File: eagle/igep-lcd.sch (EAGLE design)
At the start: 9 parts, among them IC1 LM1117IMPX-3.3, U1 SN74LVC8T245PW, U2 SN74LVC8T245PW, U3 SN74LVC8T245PW, U4 SN74LVC8T245PW

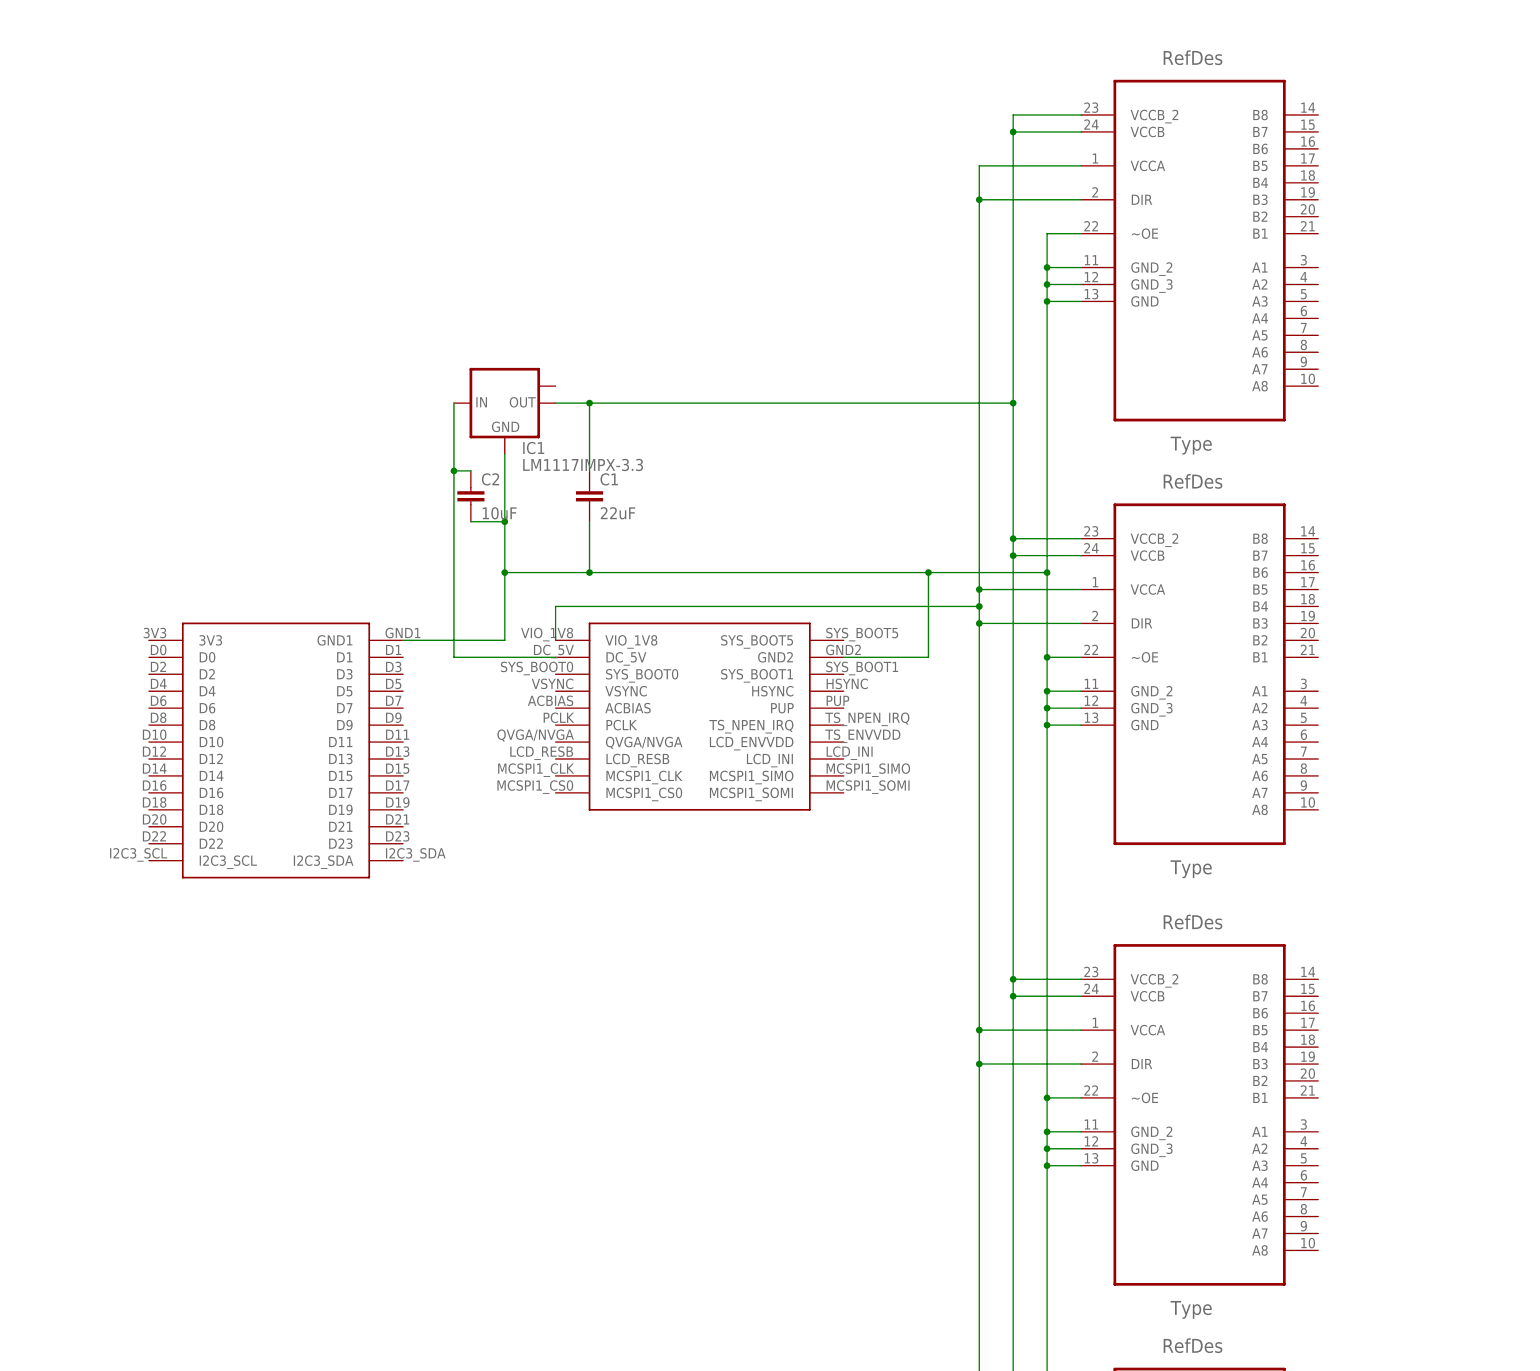
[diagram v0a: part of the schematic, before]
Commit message: Added LCD data bus to level shifters
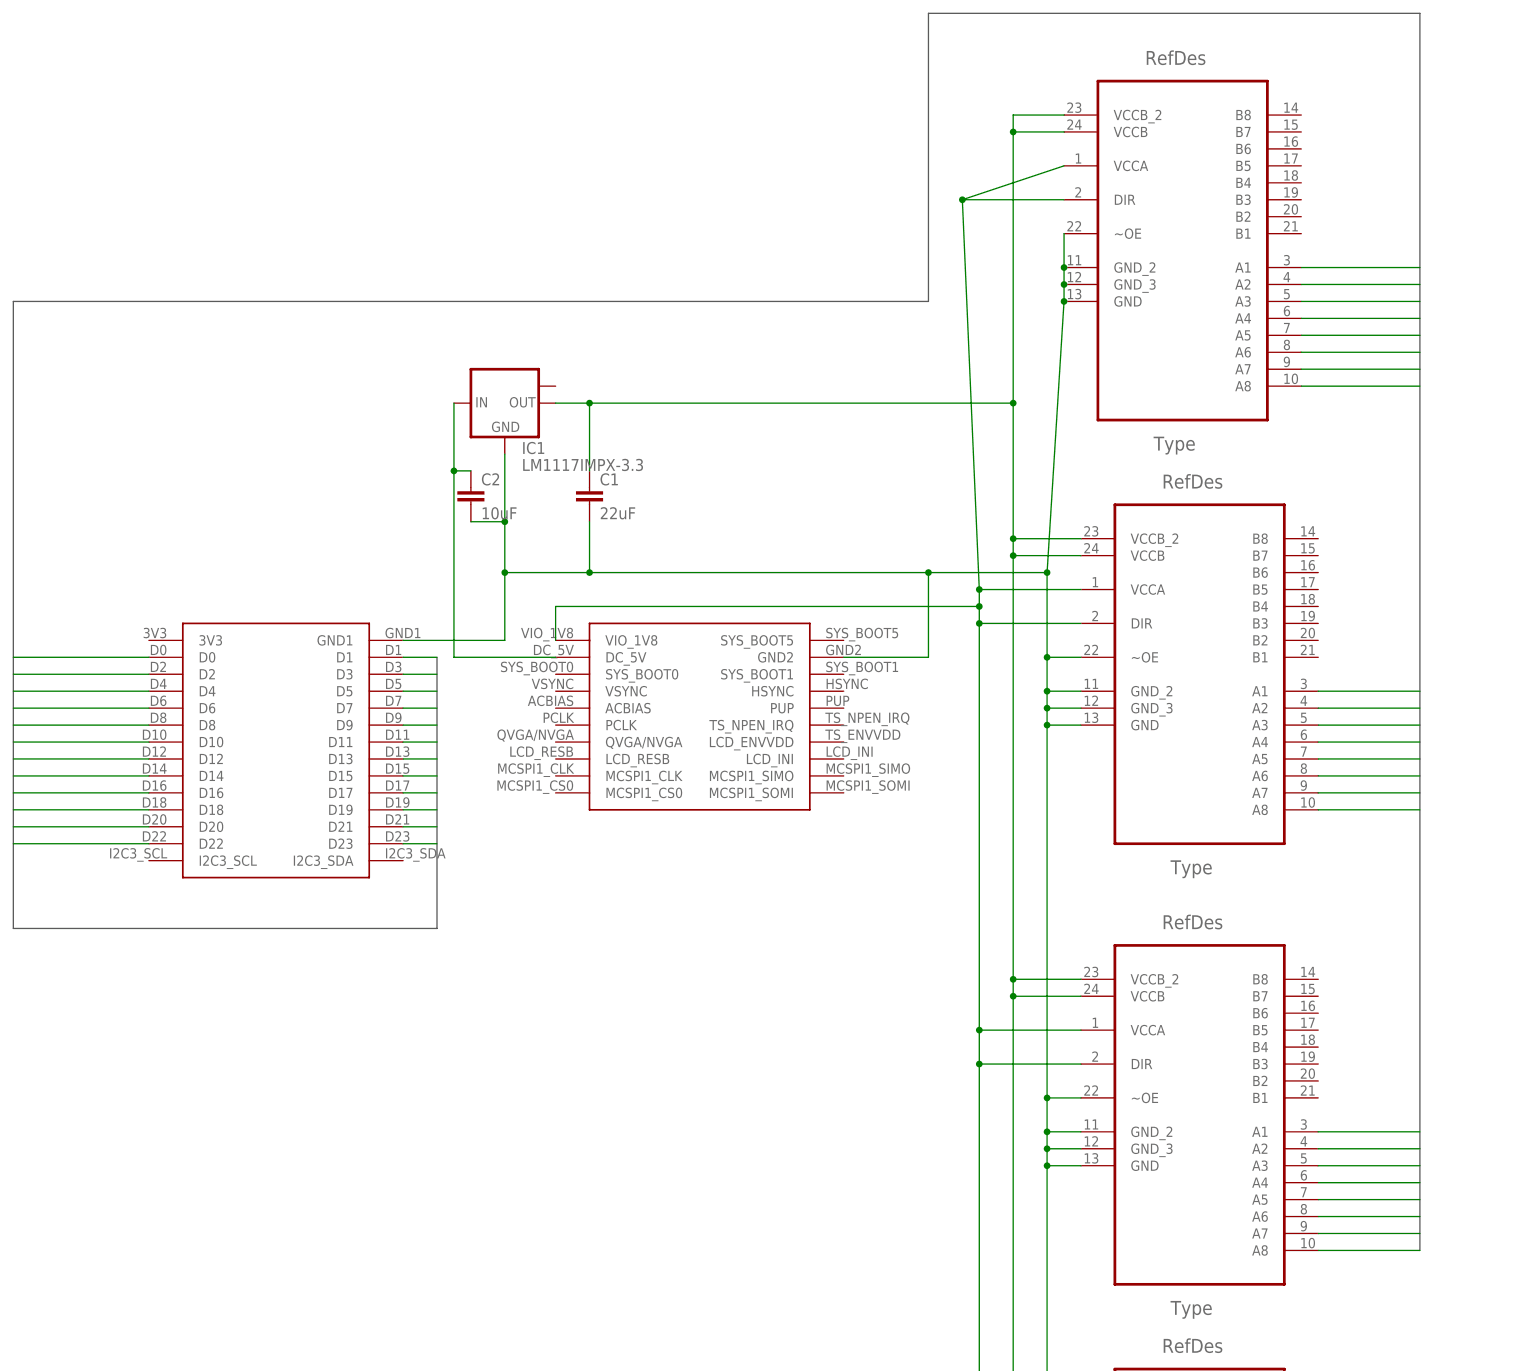
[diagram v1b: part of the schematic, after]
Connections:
- new net LCD_DATA0: U$1.D0, U1.A1
- new net LCD_DATA1: U$1.D1, U1.A2
- new net LCD_DATA10: U$1.D10, U2.A3
- new net LCD_DATA11: U$1.D11, U2.A4
- new net LCD_DATA12: U$1.D12, U2.A5
- new net LCD_DATA13: U$1.D13, U2.A6
- new net LCD_DATA14: U$1.D14, U2.A7
- new net LCD_DATA15: U$1.D15, U2.A8
- new net LCD_DATA16: U$1.D16, U3.A1
- new net LCD_DATA17: U$1.D17, U3.A2
- new net LCD_DATA18: U$1.D18, U3.A3
- new net LCD_DATA19: U$1.D19, U3.A4
- new net LCD_DATA2: U$1.D2, U1.A3
- new net LCD_DATA20: U$1.D20, U3.A5
- new net LCD_DATA21: U$1.D21, U3.A6
- new net LCD_DATA22: U$1.D22, U3.A7
- new net LCD_DATA23: U$1.D23, U3.A8
- new net LCD_DATA3: U$1.D3, U1.A4
- new net LCD_DATA4: U$1.D4, U1.A5
- new net LCD_DATA5: U$1.D5, U1.A6
- new net LCD_DATA6: U$1.D6, U1.A7
- new net LCD_DATA7: U$1.D7, U1.A8
- new net LCD_DATA8: U$1.D8, U2.A1
- new net LCD_DATA9: U$1.D9, U2.A2

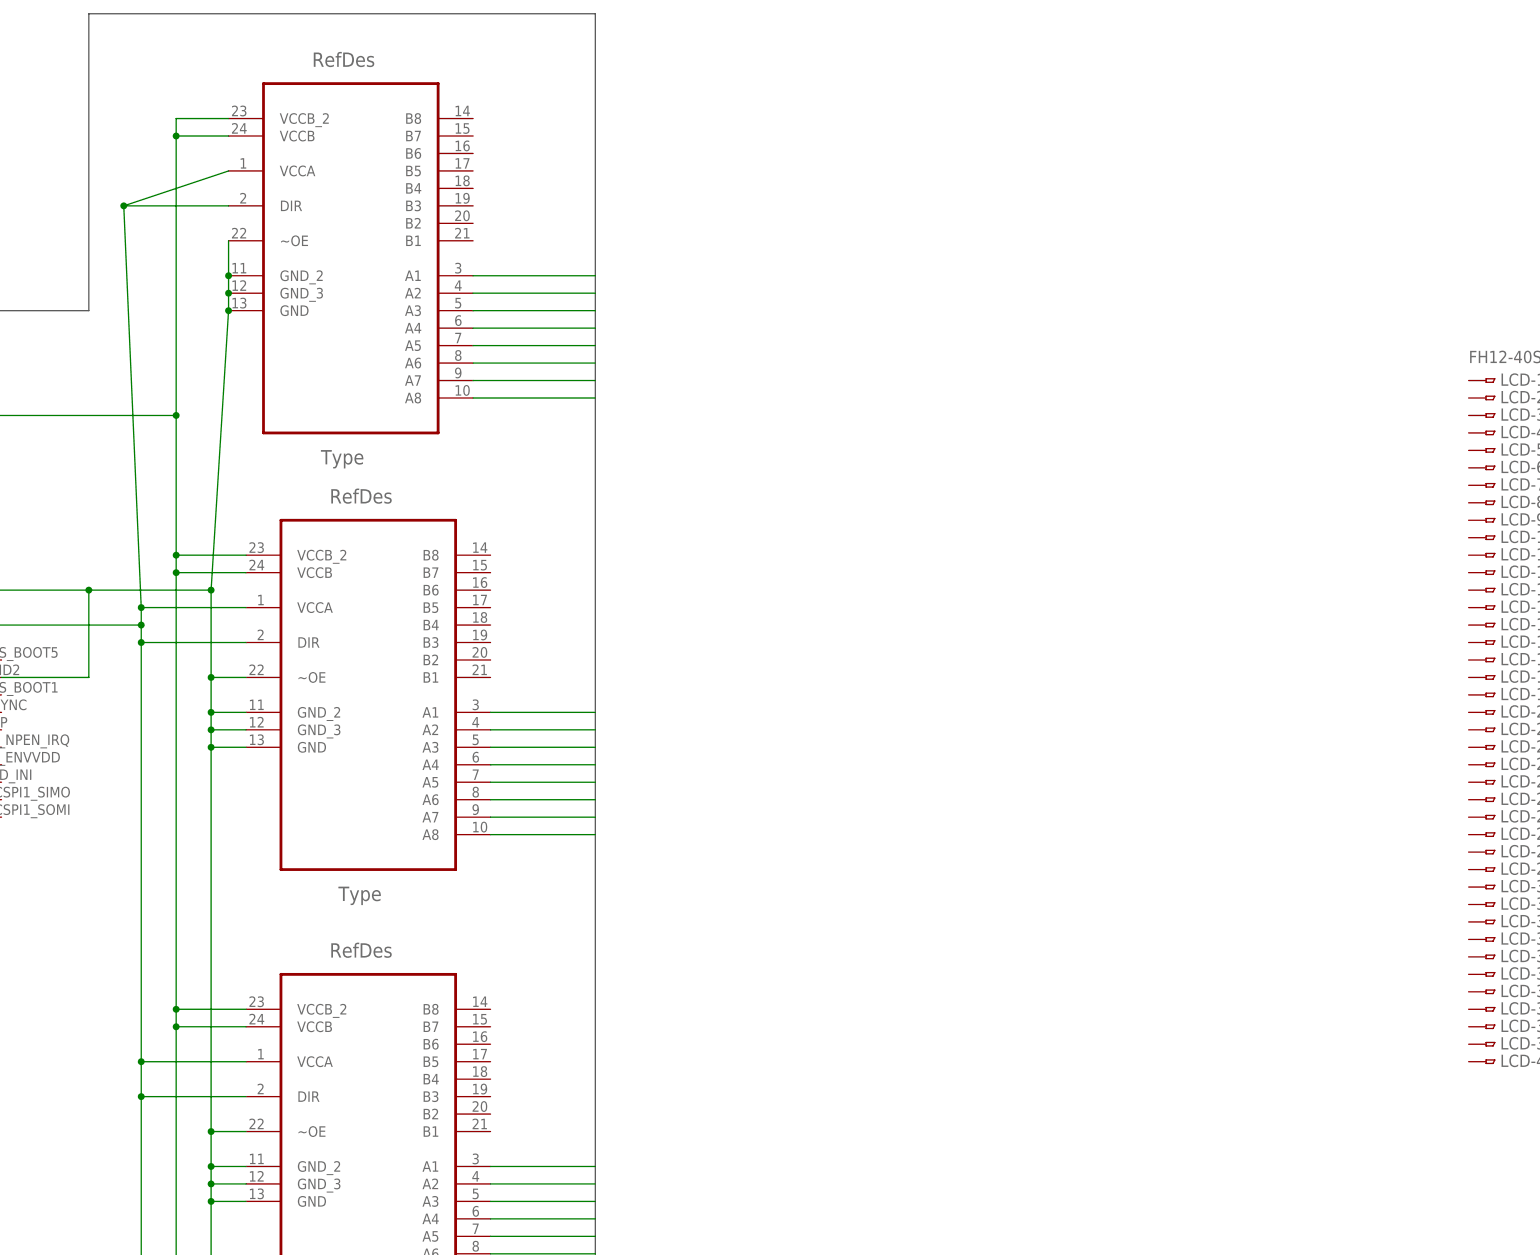
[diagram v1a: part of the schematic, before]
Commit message: Igep lcd data to level shifters
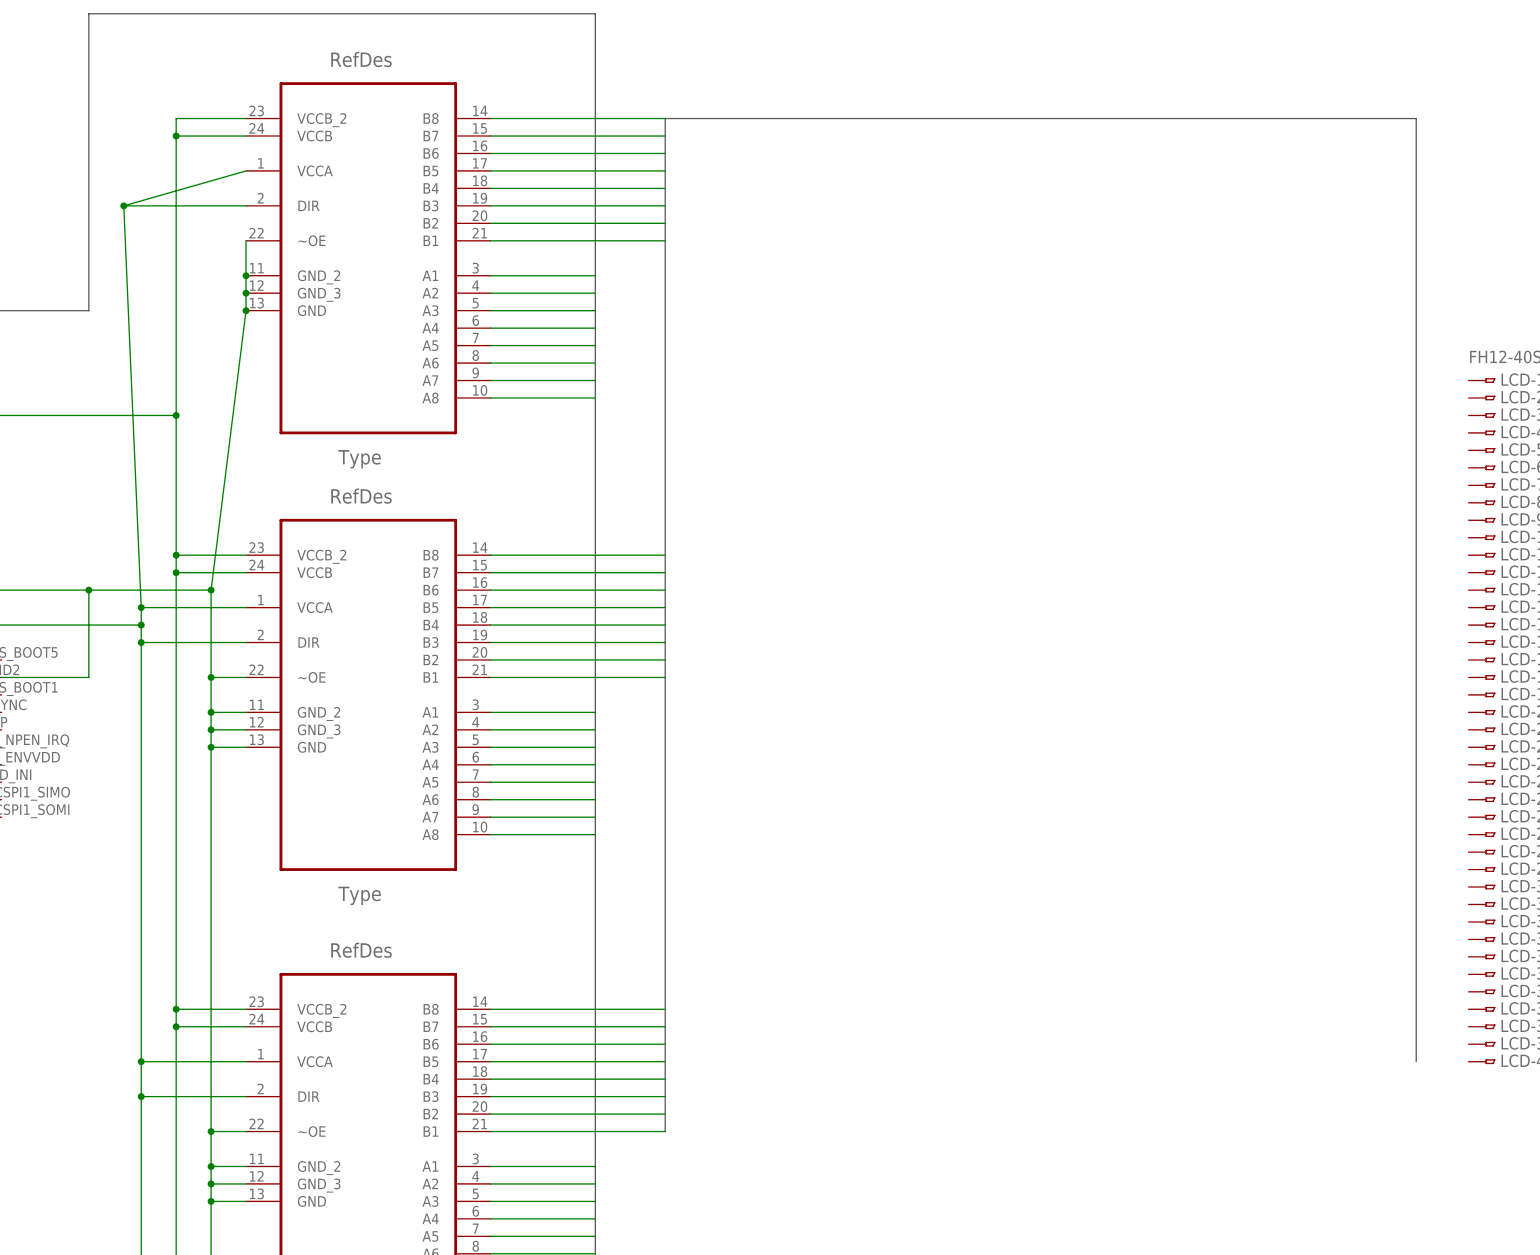
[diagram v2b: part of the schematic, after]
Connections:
- net LCD_DATA0: now also U1.B1
- net LCD_DATA1: now also U1.B2
- net LCD_DATA10: now also U2.B3
- net LCD_DATA11: now also U2.B4
- net LCD_DATA12: now also U2.B5
- net LCD_DATA13: now also U2.B6
- net LCD_DATA14: now also U2.B7
- net LCD_DATA15: now also U2.B8
- net LCD_DATA16: now also U3.B1
- net LCD_DATA17: now also U3.B2
- net LCD_DATA18: now also U3.B3
- net LCD_DATA19: now also U3.B4
- net LCD_DATA2: now also U1.B3
- net LCD_DATA20: now also U3.B5
- net LCD_DATA21: now also U3.B6
- net LCD_DATA22: now also U3.B7
- net LCD_DATA23: now also U3.B8
- net LCD_DATA3: now also U1.B4
- net LCD_DATA4: now also U1.B5
- net LCD_DATA5: now also U1.B6
- net LCD_DATA6: now also U1.B7
- net LCD_DATA7: now also U1.B8
- net LCD_DATA8: now also U2.B1
- net LCD_DATA9: now also U2.B2
